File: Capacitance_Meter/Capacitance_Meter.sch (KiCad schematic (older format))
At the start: 0 parts

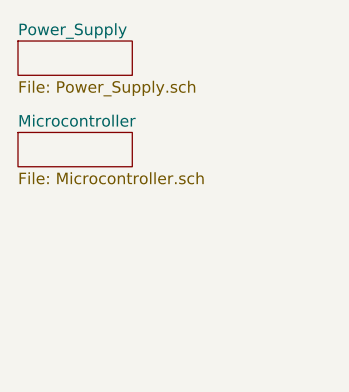
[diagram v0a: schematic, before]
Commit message: Update to capacitance meter
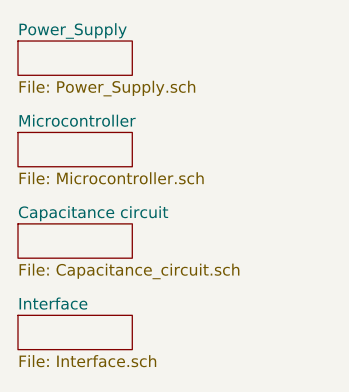
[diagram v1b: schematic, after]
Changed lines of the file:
@@
 $Descr A4 11693 8268
 encoding utf-8
-Sheet 1 3
+Sheet 1 5
 Title "Capacitance Meter"
 Date "2020-05-24"
@@
 F1 "Microcontroller.sch" 50
 $EndSheet
+$Sheet
+S 1250 2050 500  150
+U 5EDD67CE
+F0 "Capacitance circuit" 50
+F1 "Capacitance_circuit.sch" 50
+$EndSheet
+$Sheet
+S 1250 2450 500  150
+U 5EDD6869
+F0 "Interface" 50
+F1 "Interface.sch" 50
+$EndSheet
 $EndSCHEMATC
